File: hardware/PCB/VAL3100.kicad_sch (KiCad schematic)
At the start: 67 parts, among them J1 1984617, J2 Conn_01x04_Pin, J3 B4B-XH-A, J4 B4B-XH-A, J5 OSTVN02A150, J6 OSTVN02A150, Q1 AO3407A, SW7 TS-1088-AR02016, SW8 TS-1088-AR02016, U1 RT9080-33GJ5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

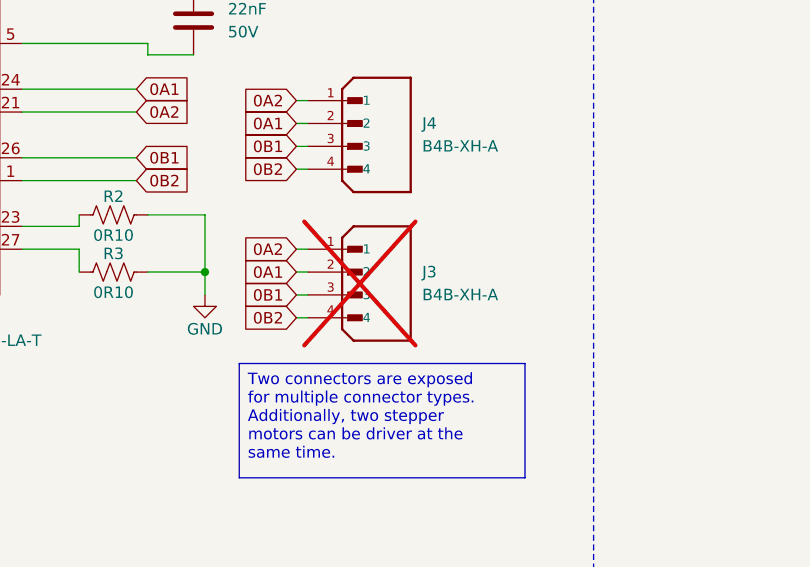
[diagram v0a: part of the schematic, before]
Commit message: Fixed 4-pin connector
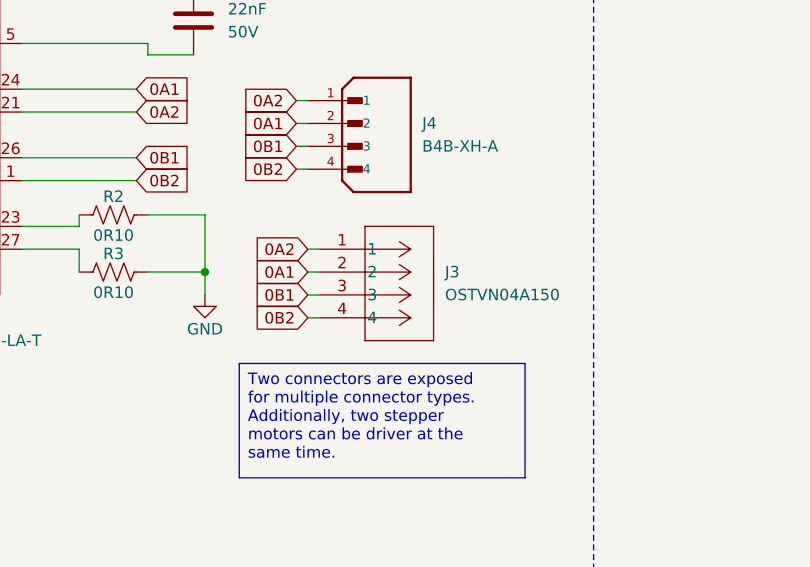
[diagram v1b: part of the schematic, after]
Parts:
- removed J3: B4B-XH-A, B4B-XH-A:JST_B4B-XH-A, symbol B4B-XH-A:B4B-XH-A
- added J3: OSTVN04A150, footprints:CONN_OSTVN04A150_OST, symbol OSTVN04A150:OSTVN04A150
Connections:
- net 0A1: now also J3.2
- net 0A2: now also J3.1
- net 0B1: now also J3.3
- net 0B2: now also J3.4
